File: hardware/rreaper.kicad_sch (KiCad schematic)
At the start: 25 parts, among them J1 ZIF, J2 USB_B_Micro, J3 ICSP, U1 ATmega328P, U2 MCP2221A, U3 74HC595, U4 74HC595, X1 16MHz

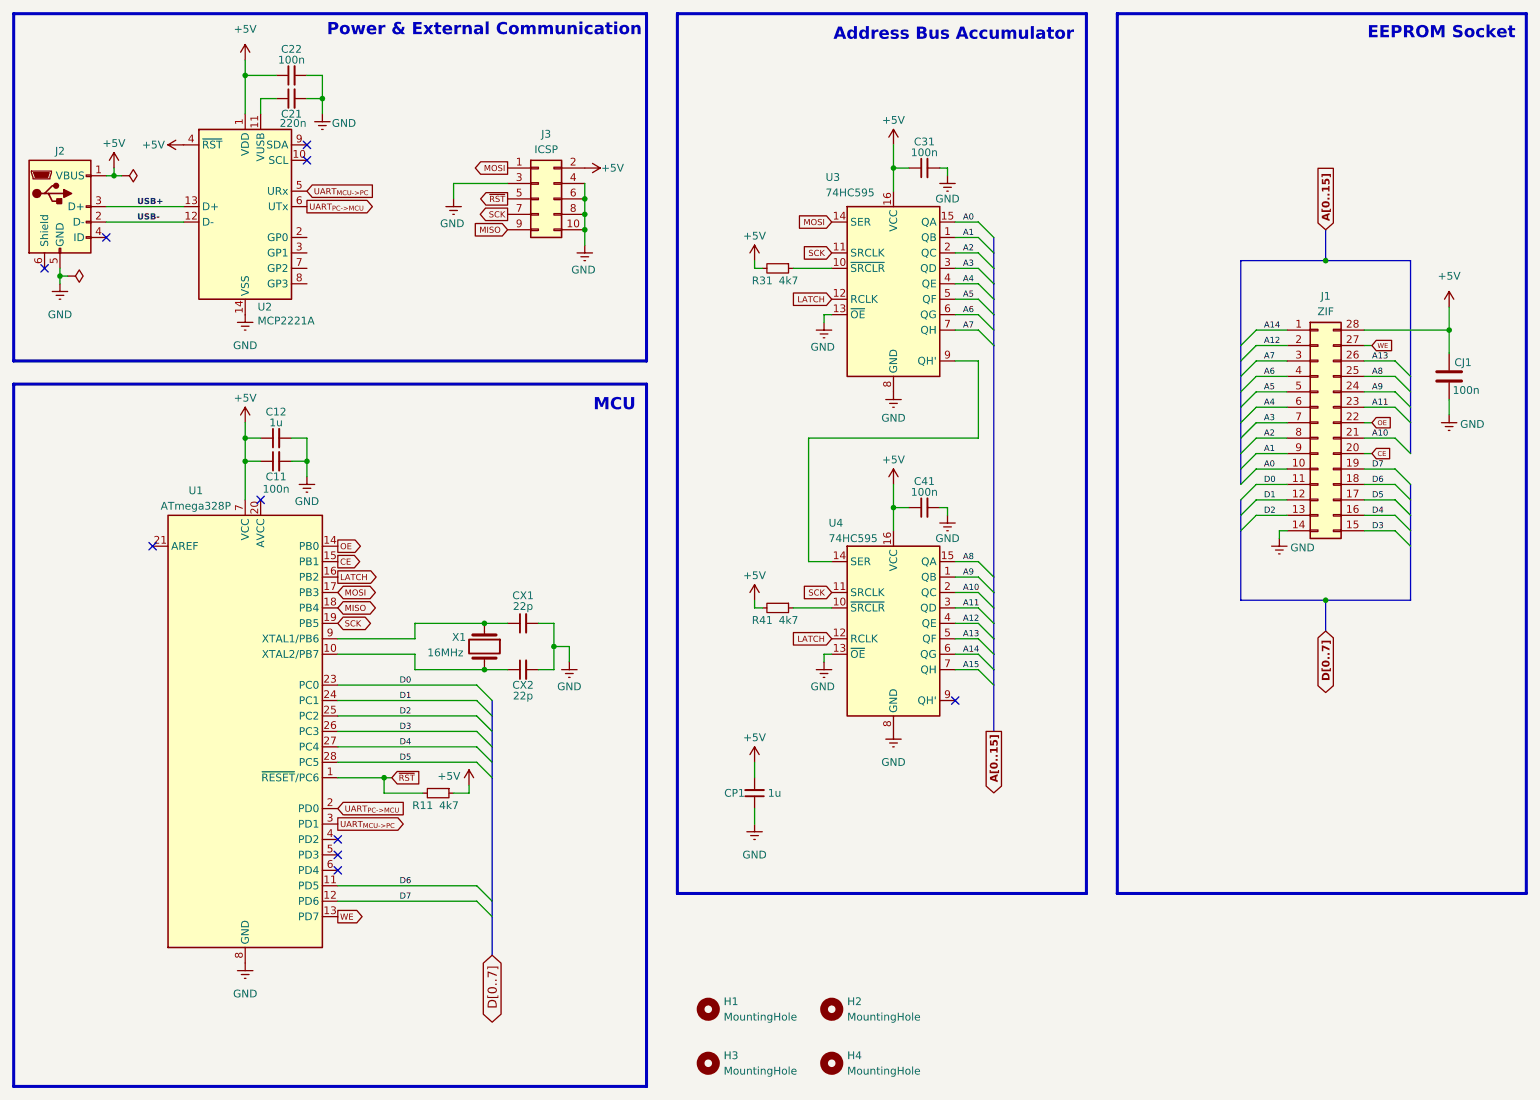
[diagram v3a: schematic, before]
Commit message: hardware: replaced USB with RS485 and external power; redesigned PCB
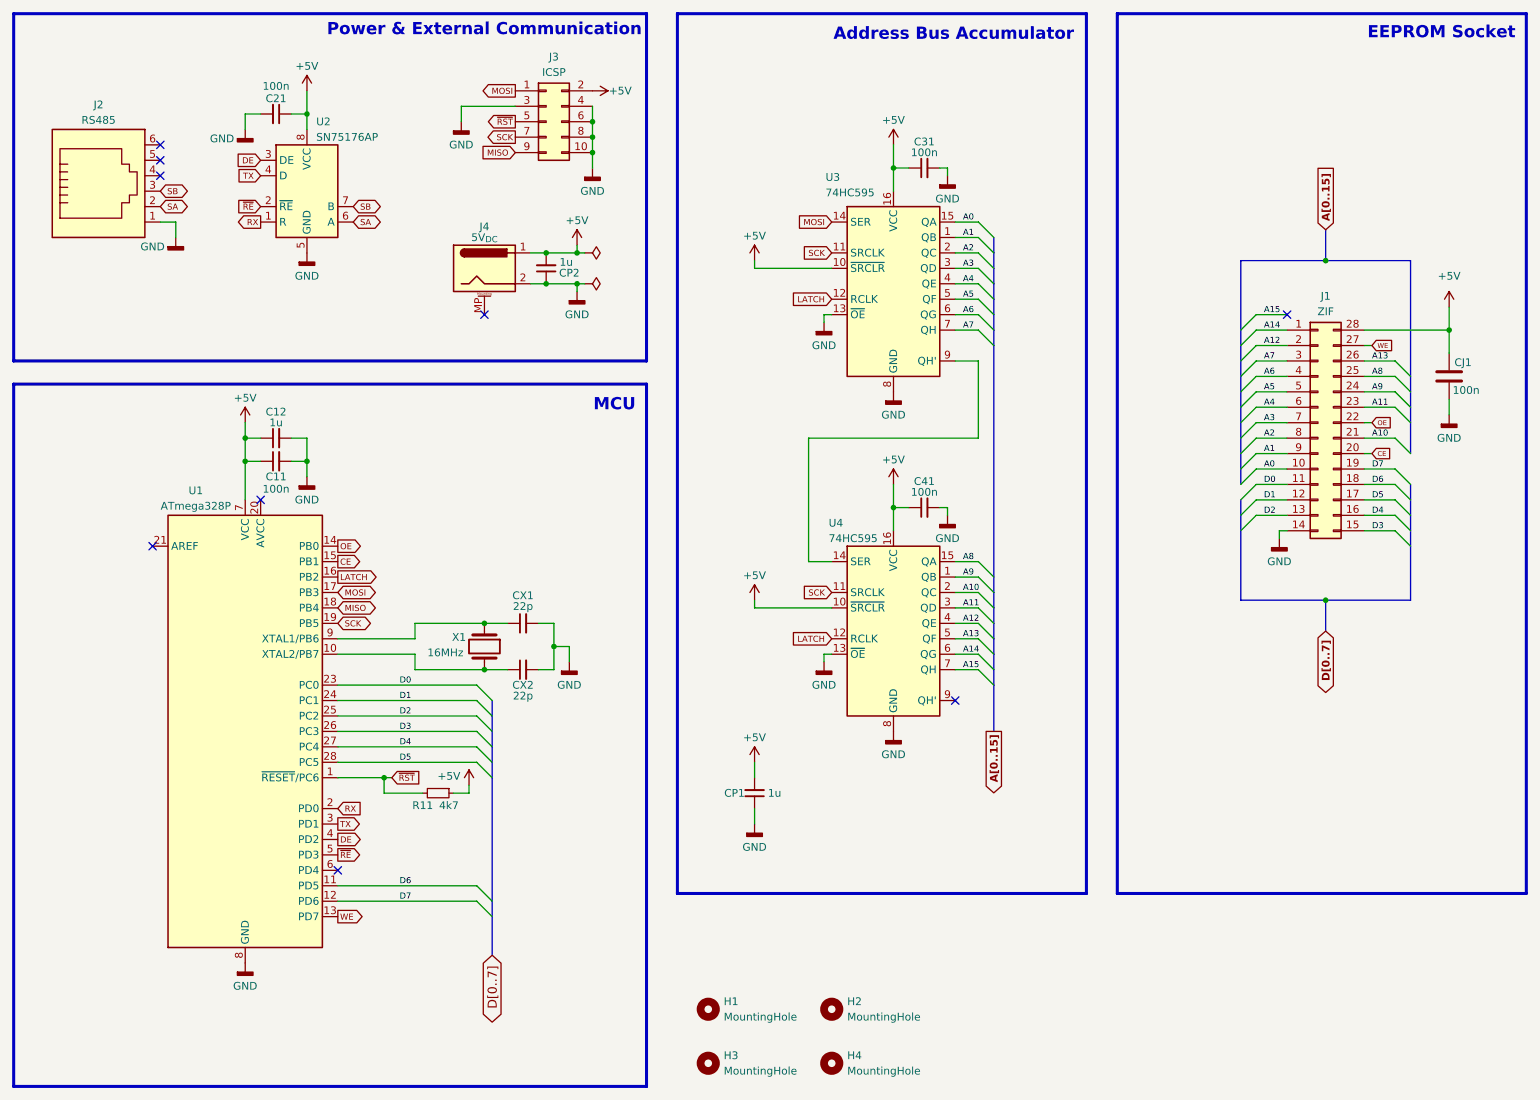
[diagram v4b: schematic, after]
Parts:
- removed C22: 100n, Capacitor_THT:C_Disc_D5.0mm_W2.5mm_P2.50mm, symbol Device:C_Small
- removed J2: USB_B_Micro, Connector_USB:USB_Micro-B_Wuerth_629105150521_CircularHoles, symbol Connector:USB_B_Micro
- removed R31, R41: 4k7, PCM_Resistor_THT_AKL:R_Axial_DIN0207_L6.3mm_D2.5mm_P10.16mm_Horizontal, symbol Device:R_Small
- removed U2: MCP2221A, PCM_Package_DIP_AKL:DIP-14_W7.62mm_Socket, symbol Interface_USB:MCP2221AxP
- added CP2: 1u, Capacitor_THT:C_Disc_D5.0mm_W2.5mm_P2.50mm, symbol Device:C_Small
- added J2: RS485, Connector_RJ:RJ12_Amphenol_54601-x06_Horizontal, symbol Connector:6P6C
- added J4: 5V_{DC}, Connector_BarrelJack:BarrelJack_GCT_DCJ200-10-A_Horizontal, symbol Connector:Barrel_Jack_MountingPin
- added U2: SN75176AP, PCM_Package_DIP_AKL:DIP-8_W7.62mm_Socket, symbol Interface_UART:SN75176AP
- C21: value 220n -> 100n
- H1, H2, H3, H4: footprint MountingHole:MountingHole_2.7mm_M2.5 -> MountingHole:MountingHole_3.2mm_M3
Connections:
- net +5V: now also C21.1, U3.10 (~{SRCLR}), U4.10 (~{SRCLR}), CP2.2, J4.1, U2.8 (VCC)
- net GND: now also CP2.1, J2.1, J4.2, U2.5 (GND)
- net DE: now reaches U1.4 (PD2)
- net DE: now also U2.3 (DE)
- net ~{RE}: now reaches U1.5 (PD3)
- net ~{RE}: now also U2.2 (~{RE})
- net UART_{MCU->PC} renamed TX
- net TX: now also U2.4 (D)
- net UART_{PC->MCU} renamed RX
- net RX: now also U2.1 (R)
- new net SA: J2.2, U2.6 (A)
- new net SB: J2.3, U2.7 (B)
- no-connect marks 10 -> 9
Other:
- moved on the sheet: J3

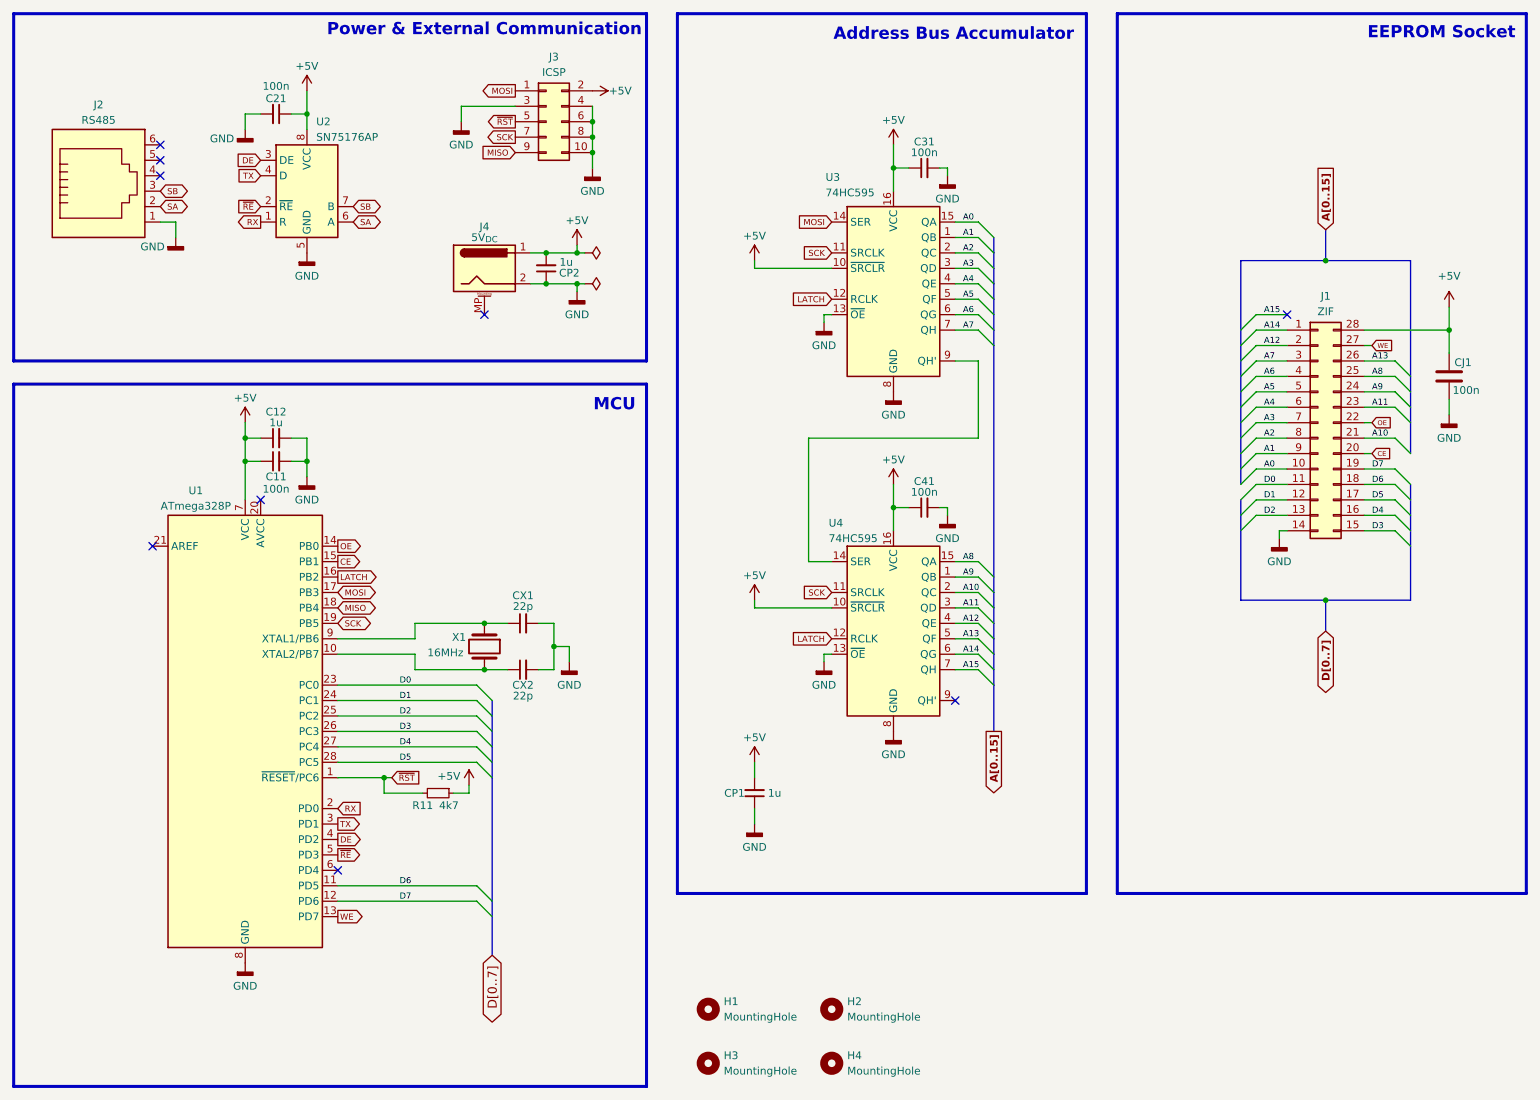
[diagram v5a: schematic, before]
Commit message: went back to USB; added serial eeprom socket; completed new layout
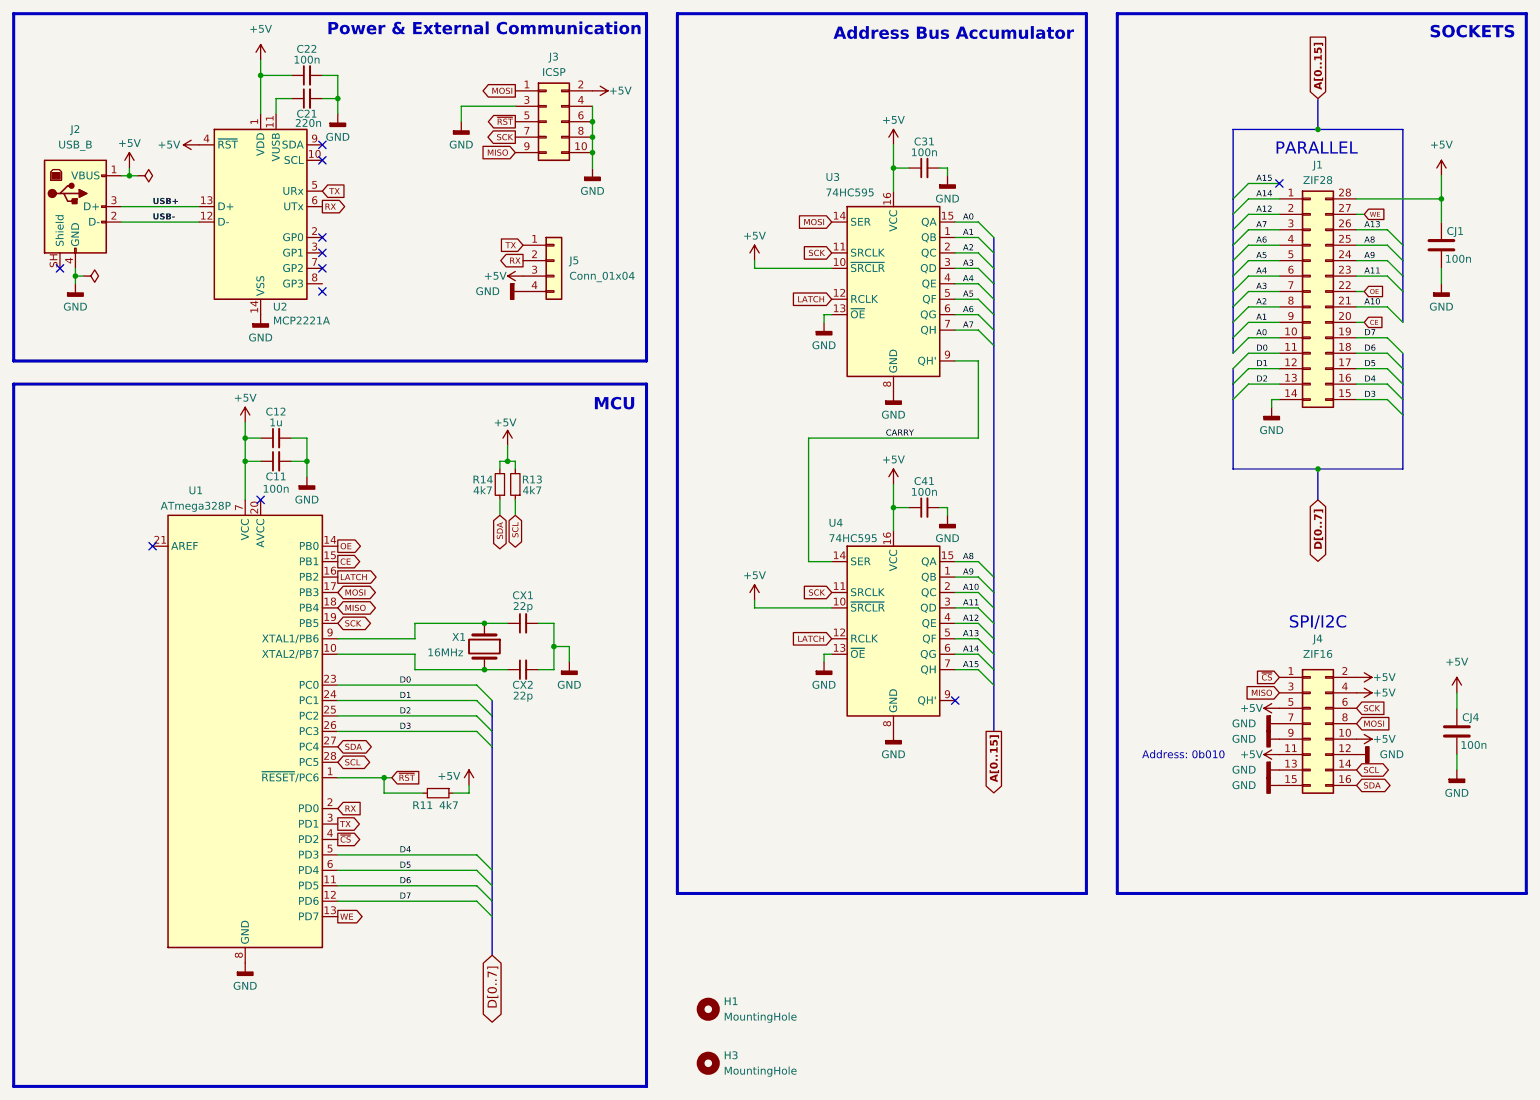
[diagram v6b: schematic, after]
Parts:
- removed CP1, CP2: 1u, Capacitor_THT:C_Disc_D5.0mm_W2.5mm_P2.50mm, symbol Device:C_Small
- removed H2, H4: MountingHole, MountingHole:MountingHole_3.2mm_M3, symbol Mechanical:MountingHole
- removed J2: RS485, Connector_RJ:RJ12_Amphenol_54601-x06_Horizontal, symbol Connector:6P6C
- removed J4: 5V_{DC}, Connector_BarrelJack:BarrelJack_GCT_DCJ200-10-A_Horizontal, symbol Connector:Barrel_Jack_MountingPin
- removed U2: SN75176AP, PCM_Package_DIP_AKL:DIP-8_W7.62mm_Socket, symbol Interface_UART:SN75176AP
- added C22: 100n, Capacitor_THT:C_Disc_D5.0mm_W2.5mm_P2.50mm, symbol Device:C_Small
- added CJ4: 100n, Capacitor_THT:C_Disc_D5.0mm_W2.5mm_P2.50mm, symbol Device:C
- added J2: USB_B, Connector_USB:USB_B_Lumberg_2411_02_Horizontal, symbol Connector:USB_B
- added J4: ZIF16, Socket:DIP_Socket-16_W4.3mm_W5.08mm_W7.62mm_W10.16mm_W10.9mm_3M_216-3340-00-0602J, symbol Connector_Generic:Conn_02x08_Odd_Even
- added J5: Conn_01x04, Connector_PinHeader_2.54mm:PinHeader_1x04_P2.54mm_Vertical, symbol Connector_Generic:Conn_01x04
- added R13, R14: 4k7, Resistor_THT:R_Axial_DIN0207_L6.3mm_D2.5mm_P7.62mm_Horizontal, symbol Device:R_Small
- added U2: MCP2221A, Package_DIP:DIP-14_W7.62mm_Socket, symbol Interface_USB:MCP2221AxP
- C21: value 100n -> 220n
- J1: value ZIF -> ZIF28; footprint Socket:DIP_Socket-28_W11.9_W12.7_W15.24_W17.78_W18.5_3M_228-1277-00-0602J -> Socket:DIP_Socket-28_W11.9mm_W12.7mm_W15.24mm_W17.78mm_W18.5mm_3M_228-1277-00-0602J
- R11: footprint PCM_Resistor_THT_AKL:R_Axial_DIN0207_L6.3mm_D2.5mm_P10.16mm_Horizontal -> Resistor_THT:R_Axial_DIN0207_L6.3mm_D2.5mm_P7.62mm_Horizontal
- U1: footprint PCM_Package_DIP_AKL:DIP-28_W7.62mm_Socket -> Package_DIP:DIP-28_W7.62mm_Socket
- U3, U4: footprint PCM_Package_DIP_AKL:DIP-16_W7.62mm_Socket -> Package_DIP:DIP-16_W7.62mm_Socket
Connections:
- net ~{RE} is gone; now on net D4: U1.5 (PD3)
- net +5V: now also C22.1, CJ4.2, J2.1 (VBUS), J4.10 (Pin_10), J4.11 (Pin_11), J4.2 (Pin_2), J4.4 (Pin_4), J4.5 (Pin_5), J5.3 (Pin_3), R13.2, R14.2, U2.1 (VDD), U2.4 (~{RST}); no longer C21.1
- net D4: no longer U1.27 (PC4)
- net D5: now also U1.6 (PD4); no longer U1.28 (PC5)
- net GND: now also C22.2, CJ4.1, J2.4 (GND), J4.12 (Pin_12), J4.13 (Pin_13), J4.15 (Pin_15), J4.7 (Pin_7), J4.9 (Pin_9), J5.4 (Pin_4), U2.14 (VSS)
- net MISO: now also J4.3 (Pin_3)
- net MOSI: now also J4.8 (Pin_8)
- net RX: now also J5.2 (Pin_2), U2.6 (UTx)
- net SCK: now also J4.6 (Pin_6)
- net TX: now also J5.1 (Pin_1), U2.5 (URx)
- net CARRY: now reaches U3.9 (QH'), U4.14 (SER)
- net DE renamed ~{CS}
- net ~{CS}: now also J4.1 (Pin_1)
- new net: C21.1, U2.11 (VUSB)
- new net SCL: J4.14 (Pin_14), R13.1, U1.28 (PC5)
- new net SDA: J4.16 (Pin_16), R14.1, U1.27 (PC4)
- new net USB+: J2.3 (D+), U2.13 (D+)
- new net USB-: J2.2 (D-), U2.12 (D-)
- no-connect marks 9 -> 11
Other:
- note added: "Address: 0b010"
- note added: "PARALLEL"
- note added: "SOCKETS"
- note added: "SPI/I2C"
- note removed: "EEPROM Socket"
- moved on the sheet: CJ1, J1

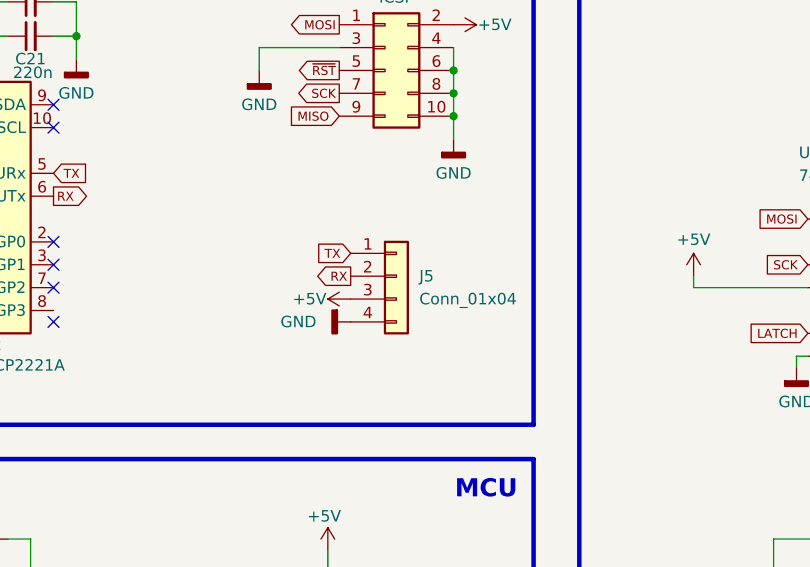
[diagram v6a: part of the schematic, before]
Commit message: added datasheets for chips used in the project; removed unused UART header from schematic
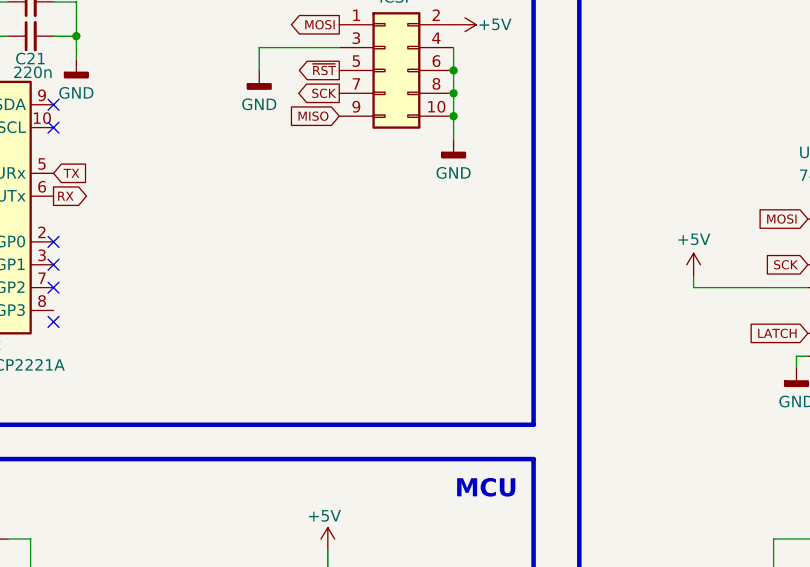
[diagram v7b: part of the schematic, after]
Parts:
- removed J5: Conn_01x04, Connector_PinHeader_2.54mm:PinHeader_1x04_P2.54mm_Vertical, symbol Connector_Generic:Conn_01x04
